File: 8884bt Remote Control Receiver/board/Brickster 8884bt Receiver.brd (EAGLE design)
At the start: 28.8 x 28.8 mm, 20 parts, among them J1 AVR_SPI_PRG_6NS, J2 CON_PF, J3 CON_PF, J4 CON_PF, U1 IC_ATTINY_X4A, U2 IC_DRV8833, U3 IC_RT9164A, U4 HC-06

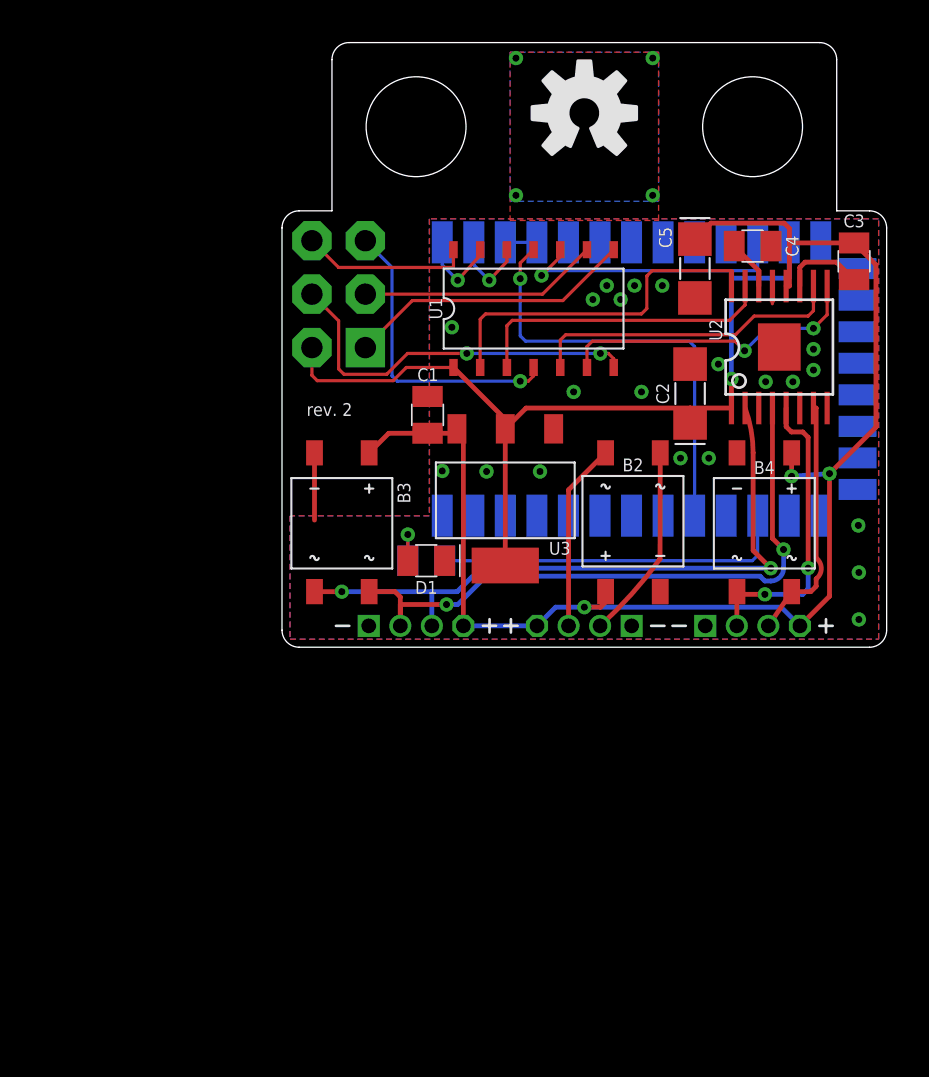
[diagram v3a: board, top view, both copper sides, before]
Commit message: Route rev. 2 board
Use SMD pads for Power Functions connections
(threading PF wire through tiny vias is too difficult)
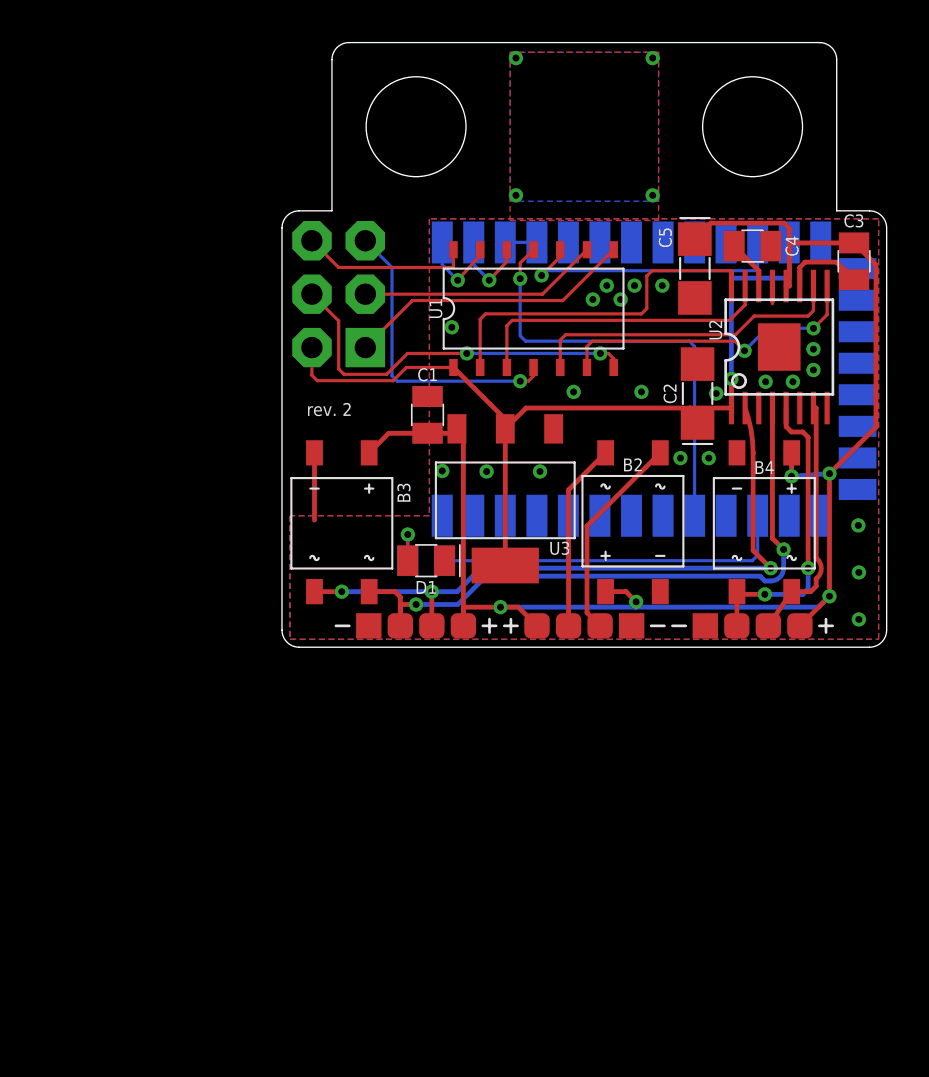
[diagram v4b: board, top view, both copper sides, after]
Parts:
- J2, J3, J4: value CON_PF -> CON_PF_SMD; device brickster:CON_PF -> brickster:SMD_PF
- LOGO1, LOGO2: device SparkFun-Aesthetics:OSHW-LOGO-M -> SparkFun-Aesthetics:OSHW-LOGO-M-MASK
- moved C2 0.36 mm to (19.8, 12.1)
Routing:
- net VIN: track 67.1 -> 71.3 mm, vias 3 -> 5
- net PF_C1: track 9.32 -> 9.93 mm
- net A01: vias 2 -> 3
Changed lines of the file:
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@@
 <attribute name="NAME" x="22.9362" y="8.2372" size="0.6096" layer="25" align="bottom-center"/>
 </element>
-<element name="LOGO1" library="SparkFun-Aesthetics" package="OSHW-LOGO-M" value="OSHW-LOGOM" x="14.3764" y="25.4"/>
+<element name="LOGO1" library="SparkFun-Aesthetics" package="OSHW-LOGO-M-MASK" value="OSHW-LOGOM" x="14.3764" y="25.4"/>
 <element name="C1" library="brickster" package="0805" value="0.1uF" x="6.9215" y="11.049" smashed="yes" rot="R270">
 <attribute name="NAME" x="6.9342" y="12.6539" size="0.6096" layer="25" align="bottom-center"/>
 </element>
-<element name="C2" library="brickster" package="1206" value="10uF" x="19.4056" y="12.065" smashed="yes" rot="R90">
-<attribute name="NAME" x="18.4056" y="12.065" size="0.6096" layer="25" rot="R90" align="bottom-center"/>
+<element name="C2" library="brickster" package="1206" value="10uF" x="19.7612" y="12.065" smashed="yes" rot="R90">
+<attribute name="NAME" x="18.7612" y="12.065" size="0.6096" layer="25" rot="R90" align="bottom-center"/>
 </element>
 <element name="C5" library="brickster" package="1206" value="10uF" x="19.6342" y="18.0086" smashed="yes" rot="R270">
 <attribute name="NAME" x="18.5326" y="19.4818" size="0.6096" layer="25" rot="R90" align="bottom-center"/>
 </element>
-<element name="J2" library="brickster" package="CON_PF" value="CON_PF" x="14.3764" y="1.016"/>
-<element name="J3" library="brickster" package="CON_PF" value="CON_PF" x="6.3754" y="1.016" rot="R180"/>
-<element name="J4" library="brickster" package="CON_PF" value="CON_PF" x="22.3774" y="1.016" rot="R180"/>
+<element name="J2" library="brickster" package="SMD_PF" value="CON_PF_SMD" x="14.3764" y="1.016"/>
+<element name="J3" library="brickster" package="SMD_PF" value="CON_PF_SMD" x="6.3754" y="1.016" rot="R180"/>
+<element name="J4" library="brickster" package="SMD_PF" value="CON_PF_SMD" x="22.3774" y="1.016" rot="R180"/>
 <element name="U2" library="brickster" package="PWP_R-PDSO-G16" value="IC_DRV8833" x="23.6474" y="14.2748" smashed="yes">
 <attribute name="NAME" x="20.9296" y="15.0876" size="0.6096" layer="21" rot="R90" align="bottom-center"/>
@@
 <attribute name="NAME" x="6.858" y="2.8448" size="0.6096" layer="21" rot="R180" align="center"/>
 </element>
-<element name="LOGO2" library="SparkFun-Aesthetics" package="OSHW-LOGO-M" value="OSHW-LOGOM" x="14.3764" y="25.4" rot="MR0"/>
+<element name="LOGO2" library="SparkFun-Aesthetics" package="OSHW-LOGO-M-MASK" value="OSHW-LOGOM" x="14.3764" y="25.4" rot="MR0"/>
 </elements>
 <signals>
@@
 <via x="15.4432" y="17.1958" extent="1-16" drill="0.3302"/>
 <via x="18.0848" y="17.1958" extent="1-16" drill="0.3302"/>
-<via x="20.7518" y="13.462" extent="1-16" drill="0.3302"/>
+<via x="20.6502" y="12.065" extent="1-16" drill="0.3302"/>
 <via x="22.9997" y="12.6238" extent="1-16" drill="0.3302"/>
 <via x="24.2951" y="12.6238" extent="1-16" drill="0.3302"/>
@@
 <via x="2.8448" y="2.6416" extent="1-16" drill="0.3302"/>
 <wire x1="2.8448" y1="2.6416" x2="7.1254" y2="2.6416" width="0.2286" layer="16"/>
-<wire x1="7.1254" y1="2.6416" x2="7.1254" y2="1.016" width="0.2286" layer="16"/>
 <wire x1="7.1254" y1="2.6416" x2="8.3312" y2="2.6416" width="0.2286" layer="16"/>
 <wire x1="8.3312" y1="2.6416" x2="9.4488" y2="3.7592" width="0.2286" layer="16"/>
@@
 <wire x1="22.4028" y1="4.5974" x2="22.4028" y2="9.2456" width="0.2286" layer="1"/>
 <wire x1="22.4028" y1="9.2456" x2="22.0224" y2="11.3748" width="0.2286" layer="1" curve="20.259027"/>
+<wire x1="7.1254" y1="1.016" x2="7.1254" y2="2.6416" width="0.2286" layer="1"/>
+<via x="7.1254" y="2.6416" extent="1-16" drill="0.3302"/>
 </signal>
 <signal name="A02">
@@
 <wire x1="5.6254" y1="2.3896" x2="5.6254" y2="1.016" width="0.2286" layer="1"/>
 <wire x1="5.6254" y1="1.016" x2="5.6254" y2="2.032" width="0.2286" layer="1"/>
-<wire x1="5.6254" y1="2.032" x2="7.8232" y2="2.032" width="0.2286" layer="1"/>
-<via x="7.8232" y="2.032" extent="1-16" drill="0.3302"/>
-<wire x1="7.8232" y1="2.032" x2="8.3566" y2="2.032" width="0.2286" layer="16"/>
+<wire x1="5.6254" y1="2.032" x2="6.3754" y2="2.032" width="0.2286" layer="1"/>
+<via x="6.3754" y="2.032" extent="1-16" drill="0.3302"/>
+<wire x1="6.3754" y1="2.032" x2="8.3566" y2="2.032" width="0.2286" layer="16"/>
 <wire x1="8.3566" y1="2.032" x2="9.7028" y2="3.3782" width="0.2286" layer="16"/>
 <wire x1="9.7028" y1="3.3782" x2="22.733" y2="3.3782" width="0.2286" layer="16"/>
@@
 <wire x1="21.3724" y1="11.3748" x2="19.4056" y2="11.3748" width="0.2286" layer="1"/>
 <wire x1="19.4056" y1="11.3748" x2="11.607" y2="11.3748" width="0.2286" layer="1"/>
-<wire x1="19.4056" y1="10.665" x2="19.4056" y2="11.3748" width="0.2286" layer="1"/>
+<wire x1="19.7612" y1="10.665" x2="19.4056" y2="11.3748" width="0.2286" layer="1"/>
 <wire x1="5.2832" y1="12.6746" x2="5.9122" y2="13.3036" width="0.1524" layer="1"/>
 <wire x1="11.607" y1="11.3748" x2="10.6172" y2="10.385" width="0.2286" layer="1"/>
@@
 <wire x1="8.6254" y1="1.016" x2="8.6254" y2="10.385" width="0.2286" layer="1"/>
 <wire x1="8.6254" y1="10.385" x2="8.3172" y2="10.385" width="0.2286" layer="1"/>
-<wire x1="8.6254" y1="1.016" x2="12.1264" y2="1.016" width="0.2286" layer="16"/>
-<wire x1="12.1264" y1="1.016" x2="13.0154" y2="1.905" width="0.2286" layer="16"/>
-<wire x1="13.0154" y1="1.905" x2="14.3764" y2="1.905" width="0.2286" layer="16"/>
-<via x="14.3764" y="1.905" extent="1-16" drill="0.3302"/>
-<wire x1="14.3764" y1="1.905" x2="15.145" y2="1.905" width="0.2286" layer="1"/>
-<wire x1="15.145" y1="1.905" x2="15.399" y2="2.159" width="0.2286" layer="1"/>
-<wire x1="15.399" y1="2.159" x2="15.3878" y2="2.6436" width="0.2286" layer="1"/>
-<wire x1="24.6274" y1="1.016" x2="23.7384" y2="1.905" width="0.2286" layer="16"/>
-<wire x1="23.7384" y1="1.905" x2="14.3764" y2="1.905" width="0.2286" layer="16"/>
+<via x="16.8402" y="2.159" extent="1-16" drill="0.3302"/>
 <wire x1="24.2362" y1="9.2436" x2="24.2316" y2="8.128" width="0.2286" layer="1"/>
 <via x="24.2316" y="8.128" extent="1-16" drill="0.3302"/>
@@
 <wire x1="23.876" y1="20.1676" x2="24.13" y2="19.9136" width="0.2286" layer="1"/>
 <wire x1="24.13" y1="19.9136" x2="24.13" y2="19.2265" width="0.2286" layer="1"/>
+<wire x1="10.3886" y1="1.905" x2="16.8148" y2="1.905" width="0.2286" layer="16"/>
+<wire x1="16.8148" y1="1.905" x2="25.5164" y2="1.905" width="0.2286" layer="16"/>
+<wire x1="15.3878" y1="2.6436" x2="16.3556" y2="2.6436" width="0.2286" layer="1"/>
+<wire x1="16.8402" y1="2.159" x2="16.8402" y2="1.9304" width="0.2286" layer="16"/>
+<wire x1="16.8402" y1="1.9304" x2="16.8148" y2="1.905" width="0.2286" layer="16"/>
+<wire x1="16.3556" y1="2.6436" x2="16.8402" y2="2.159" width="0.2286" layer="1"/>
+<wire x1="25.5164" y1="1.905" x2="26.035" y2="2.4236" width="0.2286" layer="16"/>
+<via x="26.035" y="2.4236" extent="1-16" drill="0.3302"/>
+<via x="10.3886" y="1.905" extent="1-16" drill="0.3302"/>
+<wire x1="10.3886" y1="1.905" x2="8.6254" y2="1.905" width="0.2286" layer="1"/>
+<wire x1="8.6254" y1="1.905" x2="8.6254" y2="1.016" width="0.2286" layer="1"/>
+<wire x1="10.3886" y1="1.905" x2="11.2374" y2="1.905" width="0.2286" layer="1"/>
+<wire x1="11.2374" y1="1.905" x2="12.1264" y2="1.016" width="0.2286" layer="1"/>
 </signal>
 <signal name="PF_C1">
 <contactref element="J2" pad="C1"/>
 <contactref element="B2" pad="AC1"/>
-<wire x1="17.9766" y1="4.1964" x2="17.9878" y2="9.2436" width="0.2286" layer="1"/>
-<wire x1="15.1264" y1="1.016" x2="17.9766" y2="4.1964" width="0.2286" layer="1" curve="11.5"/>
+<wire x1="15.1264" y1="1.016" x2="14.5034" y2="1.639" width="0.2286" layer="1"/>
+<wire x1="14.5034" y1="1.639" x2="14.5034" y2="5.7592" width="0.2286" layer="1"/>
+<wire x1="14.5034" y1="5.7592" x2="17.9878" y2="9.2436" width="0.2286" layer="1"/>
 </signal>
 <signal name="PF_C2">
